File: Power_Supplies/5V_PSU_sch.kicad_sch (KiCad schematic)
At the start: 7 parts, among them U3 TPS82140

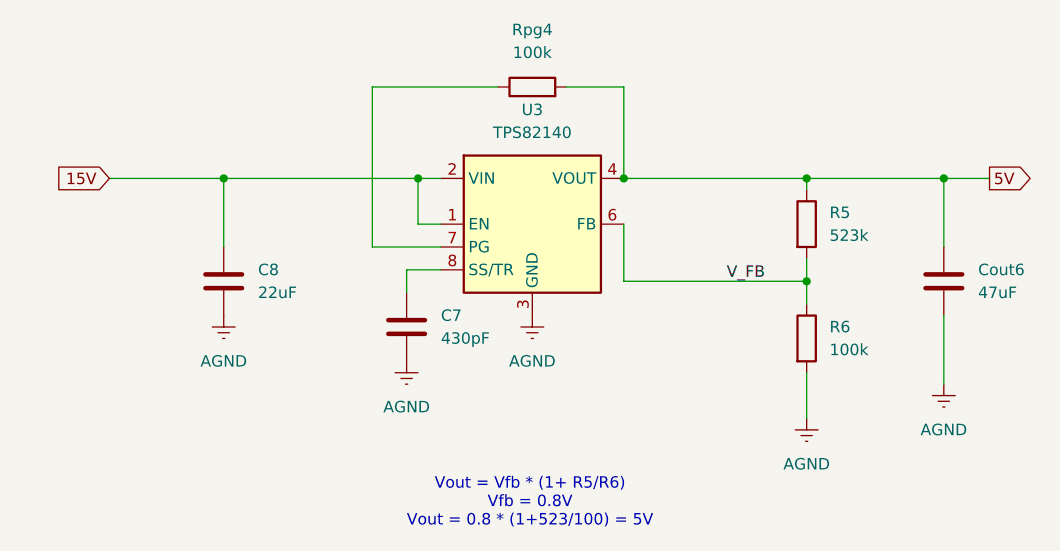
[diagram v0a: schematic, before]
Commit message: Updated power supplies and added DAC circuitry
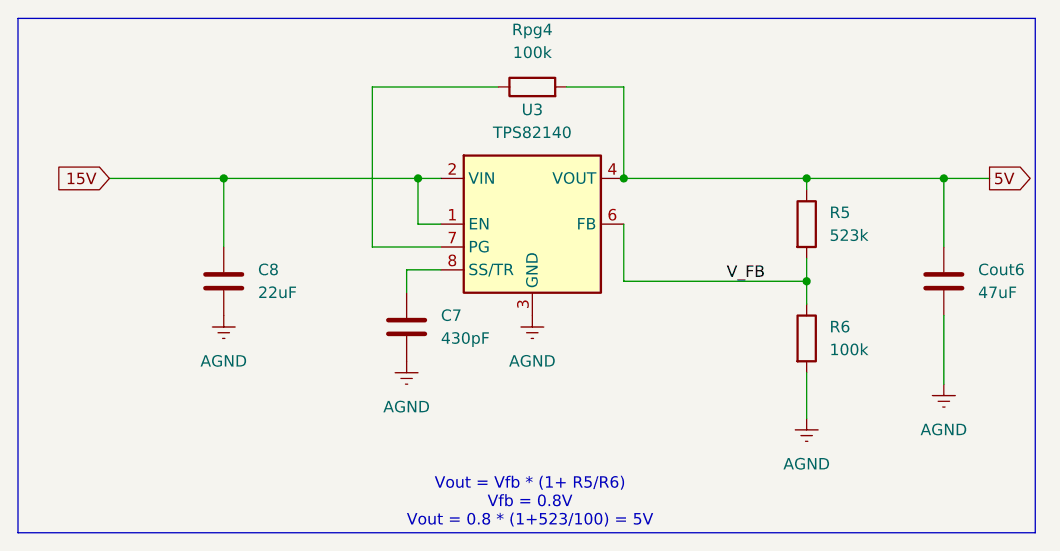
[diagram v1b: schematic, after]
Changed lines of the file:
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@@
+		)
+	)
+	(rectangle
+		(start 90.17 62.23)
+		(end 203.2 119.38)
+		(stroke
+			(width 0)
+			(type default)
+		)
+		(fill
+			(type none)
 		)
 	)

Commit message: Add files via upload
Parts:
- added C138, C139: 10uF, Capacitor_SMD:CP_Elec_4x5.8, symbol Device:C_Polarized_US
- added U24: NCP1117-5.0_SOT223, Package_TO_SOT_SMD:SOT-223-3_TabPin2, symbol Regulator_Linear:NCP1117-5.0_SOT223
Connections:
- net 15V: now also C138.1, U24.3 (VI)
- net AGND: now also C138.2, C139.2, U24.1 (GND)
- new net 5V_LDO: C139.1, U24.2 (VO)
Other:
- note added: "5V Output from Buck Converter"
- note added: "5V Output from LDO"
- note added: "NCP1117ST50T3G LDO for low noise output voltage"
- moved on the sheet: C7, C8, Cout6, R5, R6, Rpg4, U3

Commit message: big things are coming...
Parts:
- renumbered C8 to C5, C138 to C6, C139 to C8, Cout6 to Cout5, R5 to R10, R6 to R11, Rpg4 to Rpg3, U24 to U5, U3 to U6
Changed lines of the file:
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@@
+	(wire
+		(pts
+			(xy 76.2 118.11) (xy 76.2 116.84)
+		)
+		(stroke
+			(width 0)
+			(type default)
+		)
+	)
 	(wire
 		(pts
@@
 		(dnp no)
 		(fields_autoplaced yes)
-		(property "Reference" "#PWR0126"
+		(property "Reference" "#PWR014"
 			(at 62.23 123.19 0)
 			(effects
@@
 			(project "Power_Supplies"
 				(path "/5266cf9e-da90-4c53-80fd-cf3dbed42632/5982fdfd-a052-4daa-9192-d77d69fc941f"
-					(reference "#PWR0126")
+					(reference "#PWR014")
 					(unit 1)
 				)
@@
 		(dnp no)
 		(fields_autoplaced yes)
-		(property "Reference" "Cout6"
+		(property "Reference" "Cout5"
 			(at 128.27 48.2599 0)
 			(effects
@@
 			(project "Power_Supplies"
 				(path "/5266cf9e-da90-4c53-80fd-cf3dbed42632/5982fdfd-a052-4daa-9192-d77d69fc941f"
-					(reference "Cout6")
+					(reference "Cout5")
 					(unit 1)
 				)
@@
 		(dnp no)
 		(fields_autoplaced yes)
-		(property "Reference" "#PWR0127"
+		(property "Reference" "#PWR018"
 			(at 88.9 123.19 0)
 			(effects
@@
 			(project "Power_Supplies"
 				(path "/5266cf9e-da90-4c53-80fd-cf3dbed42632/5982fdfd-a052-4daa-9192-d77d69fc941f"
-					(reference "#PWR0127")
+					(reference "#PWR018")
 					(unit 1)
 				)
@@
 		(dnp no)
 		(fields_autoplaced yes)
-		(property "Reference" "#PWR015"
+		(property "Reference" "#PWR013"
 			(at 44.45 59.69 0)
 			(effects
@@
 			(project "Power_Supplies"
 				(path "/5266cf9e-da90-4c53-80fd-cf3dbed42632/5982fdfd-a052-4daa-9192-d77d69fc941f"
-					(reference "#PWR015")
+					(reference "#PWR013")
 					(unit 1)
 				)
@@
 		(dnp no)
 		(fields_autoplaced yes)
-		(property "Reference" "#PWR013"
+		(property "Reference" "#PWR017"
 			(at 78.74 59.69 0)
 			(effects
@@
 			(project "Power_Supplies"
 				(path "/5266cf9e-da90-4c53-80fd-cf3dbed42632/5982fdfd-a052-4daa-9192-d77d69fc941f"
-					(reference "#PWR013")
+					(reference "#PWR017")
 					(unit 1)
 				)
@@
 		(dnp no)
 		(fields_autoplaced yes)
-		(property "Reference" "#PWR017"
+		(property "Reference" "#PWR020"
 			(at 124.46 67.31 0)
 			(effects
@@
 			(project "Power_Supplies"
 				(path "/5266cf9e-da90-4c53-80fd-cf3dbed42632/5982fdfd-a052-4daa-9192-d77d69fc941f"
-					(reference "#PWR017")
+					(reference "#PWR020")
 					(unit 1)
 				)
@@
 		(dnp no)
 		(fields_autoplaced yes)
-		(property "Reference" "Rpg4"
+		(property "Reference" "Rpg3"
 			(at 78.74 21.59 90)
 			(effects
@@
 			(project "Power_Supplies"
 				(path "/5266cf9e-da90-4c53-80fd-cf3dbed42632/5982fdfd-a052-4daa-9192-d77d69fc941f"
-					(reference "Rpg4")
+					(reference "Rpg3")
 					(unit 1)
 				)
@@
 	(symbol
 		(lib_id "power:Earth")
-		(at 76.2 116.84 0)
-		(unit 1)
-		(exclude_from_sim no)
-		(in_bom yes)
-		(on_board yes)
-		(dnp no)
-		(fields_autoplaced yes)
-		(property "Reference" "#PWR0125"
+		(at 76.2 118.11 0)
+		(unit 1)
+		(exclude_from_sim no)
+		(in_bom yes)
+		(on_board yes)
+		(dnp no)
+		(fields_autoplaced yes)
+		(property "Reference" "#PWR016"
+			(at 76.2 124.46 0)
+			(effects
+				(font
+					(size 1.27 1.27)
+				)
+				(hide yes)
+			)
+		)
+		(property "Value" "AGND"
 			(at 76.2 123.19 0)
 			(effects
@@
 					(size 1.27 1.27)
 				)
-				(hide yes)
-			)
-		)
-		(property "Value" "AGND"
-			(at 76.2 121.92 0)
-			(effects
-				(font
-					(size 1.27 1.27)
-				)
 			)
 		)
 		(property "Footprint" ""
-			(at 76.2 116.84 0)
-			(effects
-				(font
-					(size 1.27 1.27)
-				)
-				(hide yes)
-			)
-		)
-		(property "Datasheet" "~"
-			(at 76.2 116.84 0)
+			(at 76.2 118.11 0)
+			(effects
+				(font
+					(size 1.27 1.27)
+				)
+				(hide yes)
+			)
+		)
+		(property "Datasheet" "~"
+			(at 76.2 118.11 0)
 			(effects
 				(font
@@
 		)
 		(property "Description" "Power symbol creates a global label with name \"Earth\""
-			(at 76.2 116.84 0)
-			(effects
-				(font
-					(size 1.27 1.27)
-				)
-				(hide yes)
-			)
-		)
-		(pin "1"
-		)
-		(instances
-			(project "Power_Supplies"
-				(path "/5266cf9e-da90-4c53-80fd-cf3dbed42632/5982fdfd-a052-4daa-9192-d77d69fc941f"
-					(reference "#PWR0125")
+			(at 76.2 118.11 0)
+			(effects
+				(font
+					(size 1.27 1.27)
+				)
+				(hide yes)
+			)
+		)
+		(pin "1"
+		)
+		(instances
+			(project "Power_Supplies"
+				(path "/5266cf9e-da90-4c53-80fd-cf3dbed42632/5982fdfd-a052-4daa-9192-d77d69fc941f"
+					(reference "#PWR016")
 					(unit 1)
 				)
@@
 		(dnp no)
 		(fields_autoplaced yes)
-		(property "Reference" "C8"
+		(property "Reference" "C5"
 			(at 48.26 48.2599 0)
 			(effects
@@
 			(project "Power_Supplies"
 				(path "/5266cf9e-da90-4c53-80fd-cf3dbed42632/5982fdfd-a052-4daa-9192-d77d69fc941f"
-					(reference "C8")
+					(reference "C5")
 					(unit 1)
 				)
@@
 		(on_board yes)
 		(dnp no)
-		(property "Reference" "C138"
+		(property "Reference" "C6"
 			(at 58.674 113.03 90)
 			(effects
@@
 			(project "Power_Supplies"
 				(path "/5266cf9e-da90-4c53-80fd-cf3dbed42632/5982fdfd-a052-4daa-9192-d77d69fc941f"
-					(reference "C138")
+					(reference "C6")
 					(unit 1)
 				)
@@
 		(dnp no)
 		(fields_autoplaced yes)
-		(property "Reference" "R5"
+		(property "Reference" "R10"
 			(at 111.76 41.9099 0)
 			(effects
@@
 			(project "Power_Supplies"
 				(path "/5266cf9e-da90-4c53-80fd-cf3dbed42632/5982fdfd-a052-4daa-9192-d77d69fc941f"
-					(reference "R5")
+					(reference "R10")
 					(unit 1)
 				)
@@
 		(dnp no)
 		(fields_autoplaced yes)
-		(property "Reference" "U24"
+		(property "Reference" "U5"
 			(at 76.2 102.87 0)
 			(effects
@@
 			(project "Power_Supplies"
 				(path "/5266cf9e-da90-4c53-80fd-cf3dbed42632/5982fdfd-a052-4daa-9192-d77d69fc941f"
-					(reference "U24")
+					(reference "U5")
 					(unit 1)
 				)
@@
 		(dnp no)
 		(fields_autoplaced yes)
-		(property "Reference" "#PWR014"
+		(property "Reference" "#PWR015"
 			(at 64.77 64.77 0)
 			(effects
@@
 			(project "Power_Supplies"
 				(path "/5266cf9e-da90-4c53-80fd-cf3dbed42632/5982fdfd-a052-4daa-9192-d77d69fc941f"
-					(reference "#PWR014")
+					(reference "#PWR015")
 					(unit 1)
 				)
@@
 		(dnp no)
 		(fields_autoplaced yes)
-		(property "Reference" "R6"
+		(property "Reference" "R11"
 			(at 111.76 54.6099 0)
 			(effects
@@
 			(project "Power_Supplies"
 				(path "/5266cf9e-da90-4c53-80fd-cf3dbed42632/5982fdfd-a052-4daa-9192-d77d69fc941f"
-					(reference "R6")
+					(reference "R11")
 					(unit 1)
 				)
@@
 		(dnp no)
 		(fields_autoplaced yes)
-		(property "Reference" "U3"
+		(property "Reference" "U6"
 			(at 78.74 30.48 0)
 			(effects
@@
 			(project ""
 				(path "/5266cf9e-da90-4c53-80fd-cf3dbed42632/5982fdfd-a052-4daa-9192-d77d69fc941f"
-					(reference "U3")
+					(reference "U6")
 					(unit 1)
 				)
@@
 		(dnp no)
 		(fields_autoplaced yes)
-		(property "Reference" "#PWR016"
+		(property "Reference" "#PWR019"
 			(at 109.22 71.12 0)
 			(effects
@@
 			(project "Power_Supplies"
 				(path "/5266cf9e-da90-4c53-80fd-cf3dbed42632/5982fdfd-a052-4daa-9192-d77d69fc941f"
-					(reference "#PWR016")
+					(reference "#PWR019")
 					(unit 1)
 				)
@@
 		(on_board yes)
 		(dnp no)
-		(property "Reference" "C139"
+		(property "Reference" "C8"
 			(at 85.344 113.03 90)
 			(effects
@@
 			(project "Power_Supplies"
 				(path "/5266cf9e-da90-4c53-80fd-cf3dbed42632/5982fdfd-a052-4daa-9192-d77d69fc941f"
-					(reference "C139")
-					(unit 1)
-				)
+					(reference "C8")
+					(unit 1)
+				)

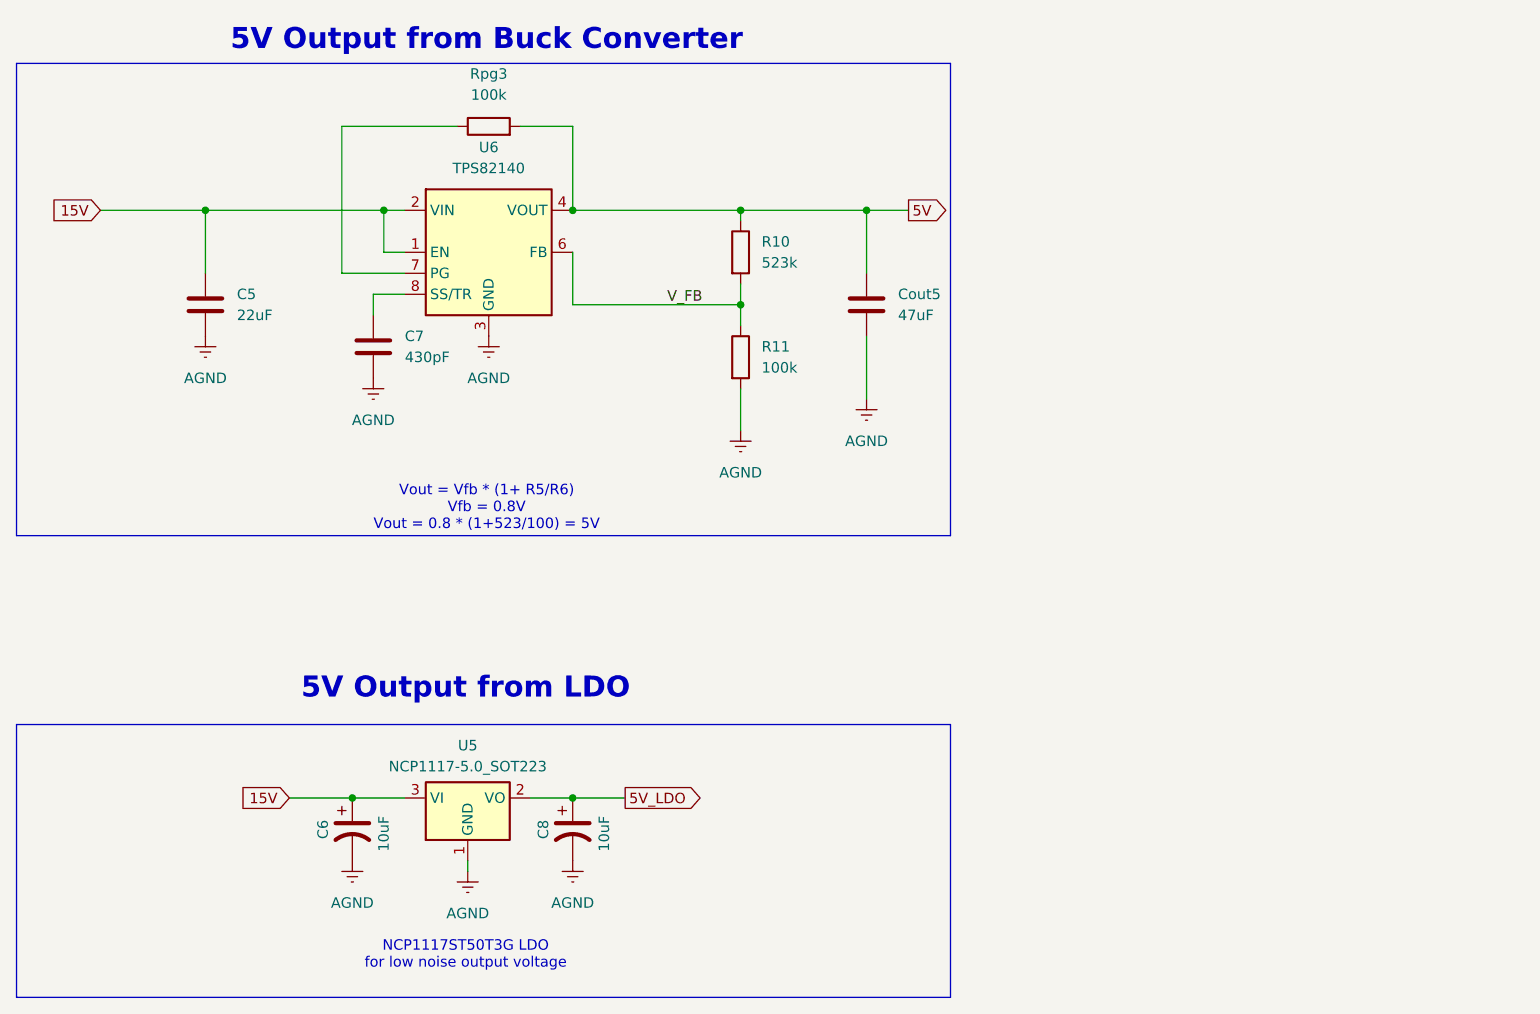
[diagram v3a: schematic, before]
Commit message: Added stuff for the power supply circuitry
changed all grounds to GND (same ground plane)
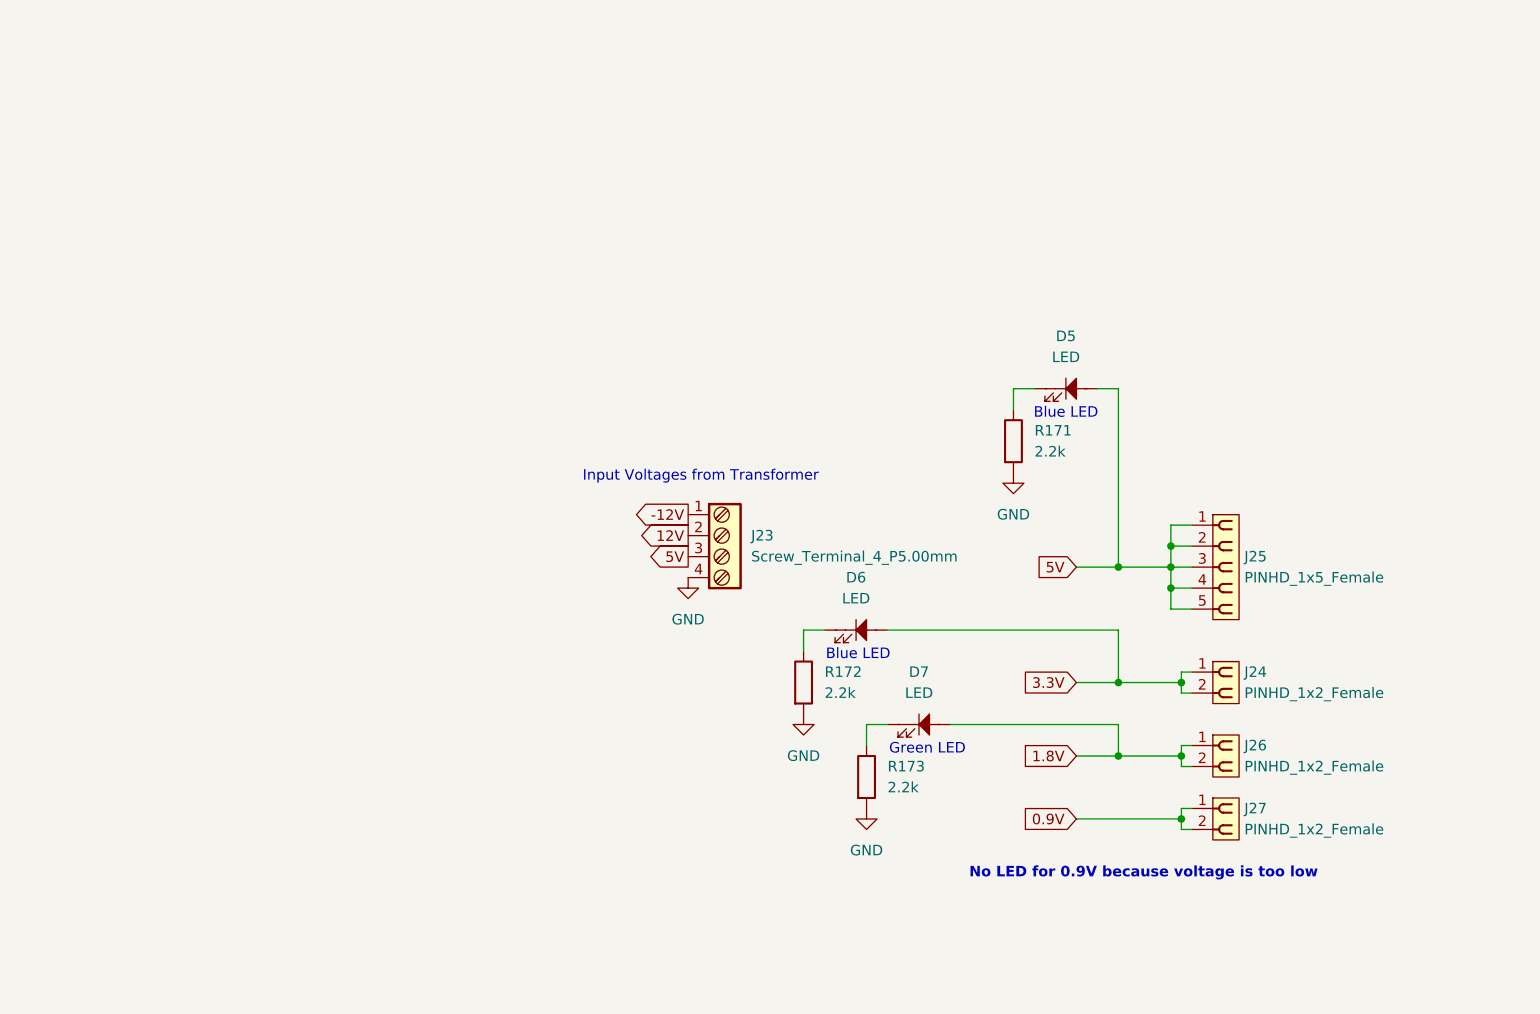
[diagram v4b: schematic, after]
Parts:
- removed C5: 22uF, Capacitor_SMD:C_0805_2012Metric, symbol Device:C
- removed C6, C8: 10uF, Capacitor_SMD:CP_Elec_4x5.8, symbol Device:C_Polarized_US
- removed C7: 430pF, Capacitor_SMD:C_0402_1005Metric, symbol Device:C
- removed Cout5: 47uF, Capacitor_SMD:C_0805_2012Metric, symbol Device:C
- removed R10: 523k, Resistor_SMD:R_0805_2012Metric, symbol Device:R
- removed R11, Rpg3: 100k, Resistor_SMD:R_0805_2012Metric, symbol Device:R
- removed U5: NCP1117-5.0_SOT223, Package_TO_SOT_SMD:SOT-223-3_TabPin2, symbol Regulator_Linear:NCP1117-5.0_SOT223
- removed U6: TPS82140, Package_LGA:Texas_SIL0008D_MicroSiP-8-1EP_2.8x3mm_P0.65mm_EP1.1x1.9mm_ThermalVias, symbol Regulator_Switching:TPS82140
- added D5, D6, D7: LED, LED_SMD:LED_0201_0603Metric, symbol PCM_SL_Devices:LED
- added J23: Screw_Terminal_4_P5.00mm, TerminalBlock_Phoenix:TerminalBlock_Phoenix_PT-1,5-4-5.0-H_1x04_P5.00mm_Horizontal, symbol PCM_SL_Screw_Terminal:Screw_Terminal_4_P5.00mm
- added J24, J26, J27: PINHD_1x2_Female, Connector_PinSocket_2.54mm:PinSocket_1x02_P2.54mm_Vertical, symbol PCM_SL_Pin_Headers:PINHD_1x2_Female
- added J25: PINHD_1x5_Female, Connector_PinSocket_2.54mm:PinSocket_1x05_P2.54mm_Vertical, symbol PCM_SL_Pin_Headers:PINHD_1x5_Female
- added R171, R172, R173: 2.2k, Resistor_SMD:R_0805_2012Metric, symbol Device:R
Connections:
- net 5V: now also D5.2, J23.3, J25.1, J25.2, J25.3, J25.4, J25.5
- new net: D6.1, R172.1
- new net: D5.1, R171.1
- new net: D7.1, R173.1
- new net -12V: J23.1
- new net 0.9V: J27.1, J27.2
- new net 1.8V: D7.2, J26.1, J26.2
- new net 12V: J23.2
- new net 3.3V: D6.2, J24.1, J24.2
- new net GND: J23.4, R171.2, R172.2, R173.2
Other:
- note added: "Blue LED"
- note added: "Green LED"
- note added: "Input Voltages from Transformer"
- note added: "No LED for 0.9V because voltage is too low"
- note removed: "5V Output from Buck Converter"
- note removed: "5V Output from LDO"
- note removed: "NCP1117ST50T3G LDO for low noise output voltage"
- note removed: "Vout = Vfb * (1+ R5/R6) Vfb = 0.8V Vout = 0.8 * (1+523/100) = 5V"
